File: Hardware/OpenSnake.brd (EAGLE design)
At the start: 25.4 x 69.8 mm, 54 parts, among them Q1 16MHZ, U1 ATMEGA328P, U2 317

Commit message: assembly sheet optimization
-just positioning names and values so they print nicely
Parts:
- U$1: value (none) -> AP2553
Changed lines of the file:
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@@
 <?xml version="1.0" encoding="utf-8"?>
 <!DOCTYPE eagle SYSTEM "eagle.dtd">
-<eagle version="9.5.2">
+<eagle version="9.6.2">
 <drawing>
 <settings>
@@
 <attribute name="NAME" x="9.900921875" y="63.0301" size="0.4064" layer="25" rot="R180"/>
 <attribute name="PROD_ID" value="CAP-00810" x="9.011921875" y="63.7286" size="1.778" layer="27" rot="R180" display="off"/>
-<attribute name="VALUE" value="0.1uF" x="10.650221875" y="65.3796" size="0.8128" layer="27" font="vector" ratio="12" rot="R180"/>
+<attribute name="VALUE" value="0.1uF" x="10.894059375" y="65.27291875" size="0.8128" layer="27" font="vector" ratio="12" rot="R180"/>
 </element>
 <element name="R2" library="SparkFun-Resistors" package="0603-RES" value="10K" x="4.445" y="31.75" smashed="yes">
 <attribute name="NAME" x="3.556" y="32.4485" size="0.4064" layer="25"/>
 <attribute name="PROD_ID" value="RES-00824" x="4.445" y="31.75" size="1.778" layer="27" display="off"/>
-<attribute name="VALUE" value="10K" x="3.3909" y="29.9974" size="0.8128" layer="27" font="vector" ratio="12"/>
+<attribute name="VALUE" value="10K" x="3.418840625" y="30.2133" size="0.8128" layer="27" font="vector" ratio="12"/>
 </element>
 <element name="C3" library="SparkFun-Capacitors" package="0603-CAP" value="0.1uF" x="17.78" y="40.20639375" smashed="yes" rot="R135">
@@
 <attribute name="NAME" x="5.334" y="33.401" size="0.4064" layer="25" font="vector" rot="R180"/>
 <attribute name="PROD_ID" value="CAP-00810" x="4.445" y="34.163" size="1.778" layer="27" rot="R180" display="off"/>
-<attribute name="VALUE" x="6.35" y="35.6616" size="0.8128" layer="27" font="vector" ratio="12" rot="R180"/>
+<attribute name="VALUE" x="6.322059375" y="35.74288125" size="0.8128" layer="27" font="vector" ratio="12" rot="R180"/>
 </element>
 <element name="U1" library="SparkFun-DigitalIC" package="TQFP32-08" value="ATMEGA328P" x="12.49860625" y="37.03139375" smashed="yes" rot="R225">
@@
 <attribute name="NAME" x="20.2946" y="43.3832" size="0.6096" layer="25" font="vector" ratio="20" rot="R270" align="bottom-center"/>
 <attribute name="PROD_ID" value="CAP-00811" x="19.1516" y="43.3832" size="1.016" layer="27" font="vector" ratio="15" rot="R270" display="off"/>
-<attribute name="VALUE" x="22.0218" y="43.4594" size="0.8128" layer="27" font="vector" ratio="12" rot="R270" align="top-center"/>
+<attribute name="VALUE" x="21.11501875" y="43.482259375" size="0.8128" layer="27" font="vector" ratio="12" rot="R270" align="top-center"/>
 </element>
 <element name="S1" library="SparkFun-Switches" package="TACTILE_SWITCH_SMD_5.2MM" value="" x="5.08" y="24.13" smashed="yes" rot="R180">
@@
 <attribute name="NAME" x="21.844" y="32.512" size="0.4064" layer="25" font="vector"/>
 <attribute name="PROD_ID" value="RES-00818" x="22.733" y="31.75" size="1.778" layer="27" display="off"/>
-<attribute name="VALUE" x="21.6408" y="30.2514" size="0.8128" layer="27" font="vector" ratio="12"/>
+<attribute name="VALUE" x="21.75001875" y="30.14218125" size="0.8128" layer="27" font="vector" ratio="12"/>
 </element>
 <element name="R3" library="SparkFun-Resistors" package="0603-RES" value="240" x="19.812" y="36.449" smashed="yes" rot="R90">
 <attribute name="NAME" x="19.05" y="35.56" size="0.4064" layer="25" font="vector" rot="R90"/>
 <attribute name="PROD_ID" value="RES-00818" x="19.812" y="36.449" size="1.778" layer="27" rot="R90" display="off"/>
-<attribute name="VALUE" x="21.4122" y="35.433" size="0.8128" layer="27" font="vector" ratio="12" rot="R90"/>
-</element>
-<element name="U$1" library="snake" package="SOT26" value="" x="12.7" y="64.77" smashed="yes" rot="R270">
+<attribute name="VALUE" x="21.336" y="35.0748625" size="0.8128" layer="27" font="vector" ratio="12" rot="R90"/>
+</element>
+<element name="U$1" library="snake" package="SOT26" value="AP2553" x="12.7" y="64.77" smashed="yes" rot="R270">
 <attribute name="NAME" x="14.478" y="64.77" size="0.6096" layer="25" font="vector" ratio="20" rot="R270" align="bottom-center"/>
-<attribute name="VALUE" x="10.922" y="64.77" size="0.6096" layer="27" font="vector" ratio="20" rot="R270" align="top-center"/>
+<attribute name="VALUE" x="13.0302" y="64.709040625" size="0.6096" layer="27" font="vector" ratio="20" rot="R270" align="top-center"/>
 </element>
 <element name="R4" library="SparkFun-Resistors" package="0603-RES" value="10K" x="14.7828" y="67.2846" smashed="yes" rot="R180">
 <attribute name="NAME" x="15.6718" y="66.5226" size="0.4064" layer="25" font="vector" rot="R180"/>
 <attribute name="PROD_ID" value="RES-00824" x="14.7828" y="67.2846" size="1.778" layer="27" rot="R180" display="off"/>
-<attribute name="VALUE" x="15.6718" y="66.421" size="0.8128" layer="27" font="vector" ratio="12" rot="R180"/>
+<attribute name="VALUE" x="16.13408125" y="68.892421875" size="0.8128" layer="27" font="vector" ratio="12" rot="R180"/>
 </element>
 <element name="R5" library="SparkFun-Resistors" package="0603-RES" value="10K" x="10.81531875" y="61.8998" smashed="yes" rot="R180">
 <attribute name="NAME" x="11.70431875" y="61.1378" size="0.4064" layer="25" font="vector" rot="R180"/>
 <attribute name="PROD_ID" value="RES-00824" x="10.81531875" y="61.8998" size="1.778" layer="27" rot="R180" display="off"/>
-<attribute name="VALUE" x="12.13611875" y="61.0108" size="0.8128" layer="27" font="vector" ratio="12" rot="R180"/>
+<attribute name="VALUE" x="12.082778125" y="61.1759" size="0.8128" layer="27" font="vector" ratio="12" rot="R180"/>
 </element>
 <element name="J2" library="SparkFun-Connectors" library_urn="urn:adsk.eagle:library:513" package="2X3" package3d_urn="urn:adsk.eagle:package:38016/1" value="" x="6.35" y="58.42" smashed="yes" rot="MR270">
@@
 <attribute name="NAME" x="6.1976" y="62.992" size="0.4064" layer="25" font="vector" rot="R180"/>
 <attribute name="PROD_ID" value="RES-00818" x="5.3086" y="53.594" size="3.81" layer="27" font="vector" ratio="13" rot="R180" display="off"/>
-<attribute name="VALUE" x="6.3246" y="64.897" size="0.4064" layer="27" font="vector" rot="R180"/>
+<attribute name="VALUE" x="6.512559375" y="62.9412" size="0.8128" layer="27" font="vector" ratio="12" rot="R180"/>
 </element>
 <element name="D1" library="SparkFun-LED" package="LED_5MM" value="GREEN" x="8.89" y="68.58" smashed="yes">
 <attribute name="NAME" x="8.89" y="71.9709" size="0.6096" layer="25" font="vector" ratio="20" align="bottom-center"/>
-<attribute name="VALUE" x="8.9154" y="65.1891" size="0.6096" layer="27" font="vector" ratio="20" align="top-center"/>
+<attribute name="VALUE" x="8.99668125" y="67.365878125" size="0.6096" layer="27" font="vector" ratio="20" align="top-center"/>
 </element>
 </elements>

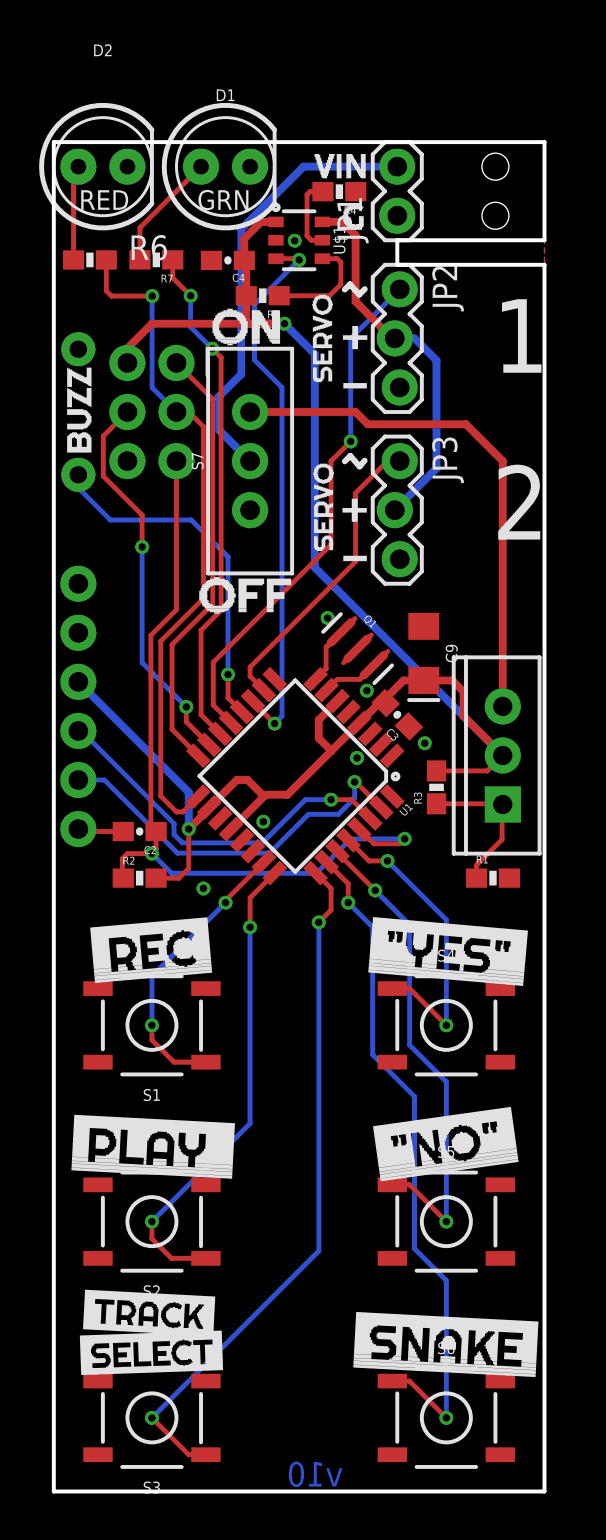
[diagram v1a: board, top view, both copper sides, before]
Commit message: v20 PCB layout - all SMD
-Moved to high side switch with mosfet for servo power control, this will also come directly from battery (since it is now max 6V) to alleviate vreg
-Switched to JST connector for batter input.
-removed power switch, because the plan is to source a battery holder with switch.
-moved to MIC5205 5V vreg, because it no longer has to power servo.
-switched to test points for programming to make room.
-SMD buzzer
-SMD LEDs
-SMD servo connectors
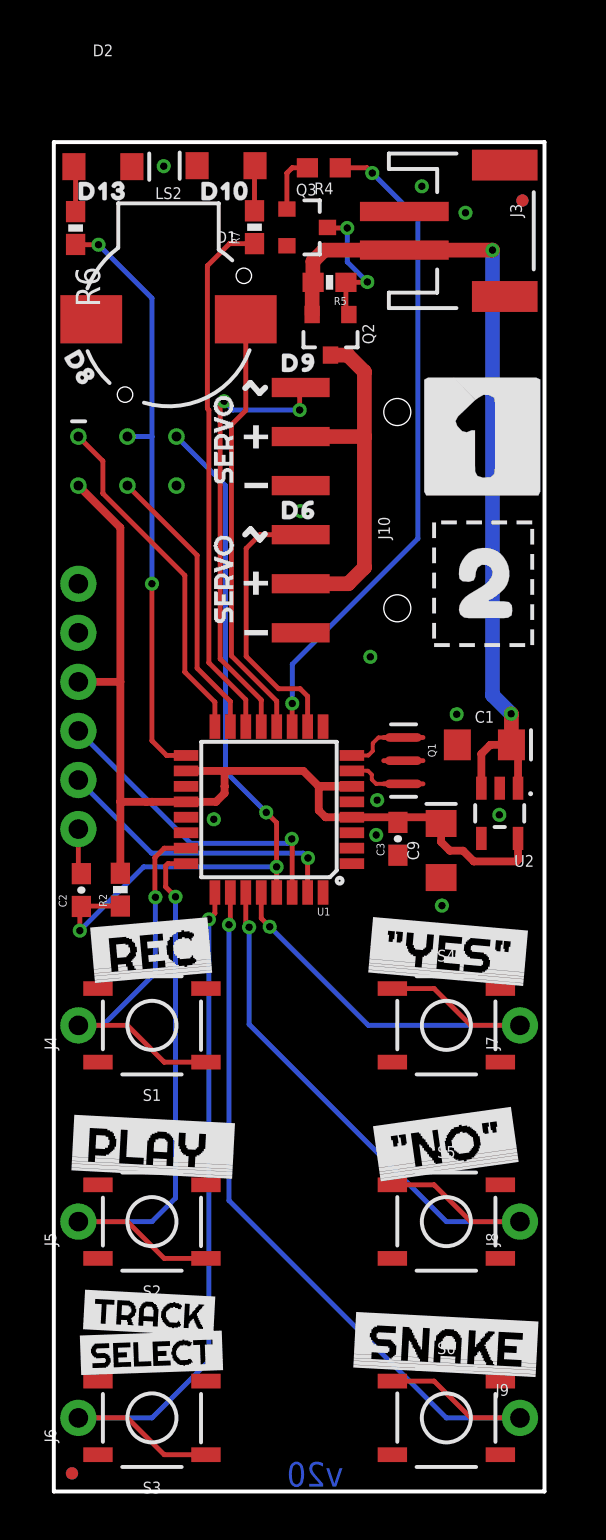
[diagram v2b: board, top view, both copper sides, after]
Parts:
- removed C4: 0.1uF, SparkFun-Capacitors:0603-CAP
- removed JP1: (no value), Testing:1X02
- removed JP2: Servo 1, Testing:1X03_LOCK
- removed JP3: Servo 2, Testing:1X03_LOCK
- removed LS1: BUZZER, SparkFun-Electromechanical:BUZZER-12MM
- removed R1: 715, SparkFun-Resistors:0603-RES
- removed R3: 240, SparkFun-Resistors:0603-RES
- removed S7: (no value), SparkFun-Switches:SWITCH_SPDT_PTH_11.6X4.0MM
- added C1: 10uF, SparkFun-Capacitors:EIA3216
- added FD1, FD2, FD3, FD4: FIDUCIALUFIDUCIAL, SparkFun-Aesthetics:FIDUCIAL-MICRO
- added J10: RA 6Pin SMD, SparkFun-Connectors:1X06-SMD_RA_MALE
- added J3: (no value), SparkFun-Connectors:JST-2-SMD
- added J4, J5, J6, J7, J8, J9: (no value), SparkFun-Connectors:1X01_NO_SILK
- added LS2: BUZZER, SparkFun-Electromechanical:BUZZER-CCV
- added Q2: 20V/4.2A/52mΩ/1.4W, SparkFun-DiscreteSemi:SOT23-3
- added Q3: 600mA/40V, SparkFun-DiscreteSemi:SOT23-3
- added U$25: (no value), output:D60
- added U$26: (no value), output:D100
- added U$27: (no value), output:D130
- added U$28: (no value), output:D80
- added U$29: (no value), output:#1#0
- added U$31: (no value), output:2_0
- added U$6: (no value), output:#A1#0
- D1, D2: device SparkFun-LED:LED_5MM -> SparkFun-LED:LED-1206
- J2: value (none) -> SPI; device SparkFun-Connectors:2X3 -> SparkFun-Connectors:2X3_TEST_POINTS
- R4: value 10K -> 120; device SparkFun-Resistors:0603-RES -> SparkFun-Resistors:0603
- U$1: value AP2553 -> (none); device snake:SOT26 -> output:#A0#0
- U$10: device buzzard_labels (1):OFF1 -> output:#A4#0
- U$17: device buzzard_labels (1):VIN6 -> output:#A5#0
- U$18: device buzzard_labels (1):G8 -> output:D90
- U$7: device buzzard_labels (4):BUZZ0 -> output:#A2#0
- U$9: device buzzard_labels (1):ON0 -> output:#A3#0
- U2: value 317 -> 5V; device SparkFun-IC-Power:TO220-ADJ -> SparkFun-IC-Power:SOT23-5
- moved U$9 59.2 mm to (24.1, 3.81), flipped to the bottom
- moved U$7 48.8 mm to (1.27, 3.81), flipped to the bottom, turned to 0 degrees
- moved U$17 46.1 mm to (24.1, 24.1), flipped to the bottom
- moved U$1 42.2 mm to (1.27, 24.1), flipped to the bottom, turned to 0 degrees
- moved U$5 39.0 mm to (25.4, 51.1)
- moved U$10 37.2 mm to (24.1, 14.0), flipped to the bottom
- moved U$14 36.2 mm to (19.7, 43.6)
- moved U$24 33.8 mm to (14.5, 40.5)
- moved U$16 33.6 mm to (22.0, 40.7)
- moved U$23 33.4 mm to (17.8, 41.0)
- moved U$15 33.0 mm to (23.2, 38.0), turned to 357 degrees
- moved LOGO1 31.8 mm to (12.7, 8.89)
- moved C9 10.2 mm to (20.0, 33.2), turned to 90 degrees
- moved U$18 7.70 mm to (12.7, 58.4)
- moved U$8 7.33 mm to (8.75, 51.2)
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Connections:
- removed net N$3: R1.1, R3.1, U2.ADJ
- removed net N$8: R4.2, U$1.5
- removed net N$9: R5.1, U$1.4
- new net VBAT: C1.+, J3.2, Q2.2, R5.2, U2.1, U2.3
- net BUZZER: now also LS2.-; no longer LS1.+
- net ENABLE_SERVO: now also R4.1; no longer U$1.3
- net GND: now also C1.-, D1.C, D2.C, J10.1, J10.4, J3.1, LS2.+, Q3.2, U2.2; no longer C4.2, D1.K, D2.K, JP1.1, JP2.3, JP3.3, LS1.-, R1.2, R4.1, U$1.2
- net N$4: now also Q3.1, R4.2; no longer JP1.2, S7.2
- net N$5: now also Q2.1, Q3.3, R5.1; no longer S7.1, U2.IN
- net N$6: now also J10.2, J10.5, Q2.3; no longer JP2.2, JP3.2, U$1.6
- net NO: now also J8.1
- net PLAY: now also J5.1
- net REC: now also J4.1
- net SERVO_1: now also J10.6; no longer JP2.1
- net SERVO_2: now also J10.3; no longer JP3.1
- net SNAKE: now also J9.1
- net TRCK_SEL: now also J6.1
- net VCC: now also U2.5; no longer C4.1, R3.2, R5.2, U$1.1, U2.OUT
- net YES: now also J7.1
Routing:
- net VBAT: track 0.00 -> 44.2 mm, vias 0 -> 2
- net VCC: track 91.3 -> 55.3 mm, vias 2 -> 0
- net N$5: track 26.8 -> 7.11 mm, vias 0 -> 2
- net N$4: track 22.6 -> 3.04 mm
- net YES: track 15.8 -> 24.4 mm, vias 2 -> 1
- net SNAKE: track 34.9 -> 43.1 mm, vias 2 -> 1
- net N$3: track 7.84 -> 0.00 mm
- net NO: track 25.1 -> 32.5 mm, vias 2 -> 1
- net PLAY: track 24.8 -> 31.4 mm, vias 2 -> 1
- net N$9: track 5.62 -> 0.00 mm
- net ENABLE_SERVO: track 28.6 -> 34.1 mm
- net REC: track 14.9 -> 20.3 mm, vias 2 -> 1
- net MOSI: track 20.0 -> 14.7 mm, vias 2 -> 0
- net MISO: track 22.5 -> 17.9 mm
- net TX: track 19.8 -> 15.4 mm
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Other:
- outline, holes or cut-outs redrawn
- board text added: "NPN"
- board text added: "PCH-DMG2305"
- board text added: "cable to 6V Battery (4xAA pack)"
- board text added: "v20"
- board text removed: "1"
- board text removed: "2"
- board text removed: "9V Battery"
- board text removed: "GRN"
- board text removed: "cable to 9V battery"
- board text removed: "v10"
